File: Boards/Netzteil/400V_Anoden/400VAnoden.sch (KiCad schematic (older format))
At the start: 48 parts, among them P1 Drossel, P2 320V_AC, P3 Stabi, P4 133V_AC, P5 Stabi, P6 Trafo, P7 Trafo, P8 Relay, Q1 2SC2979

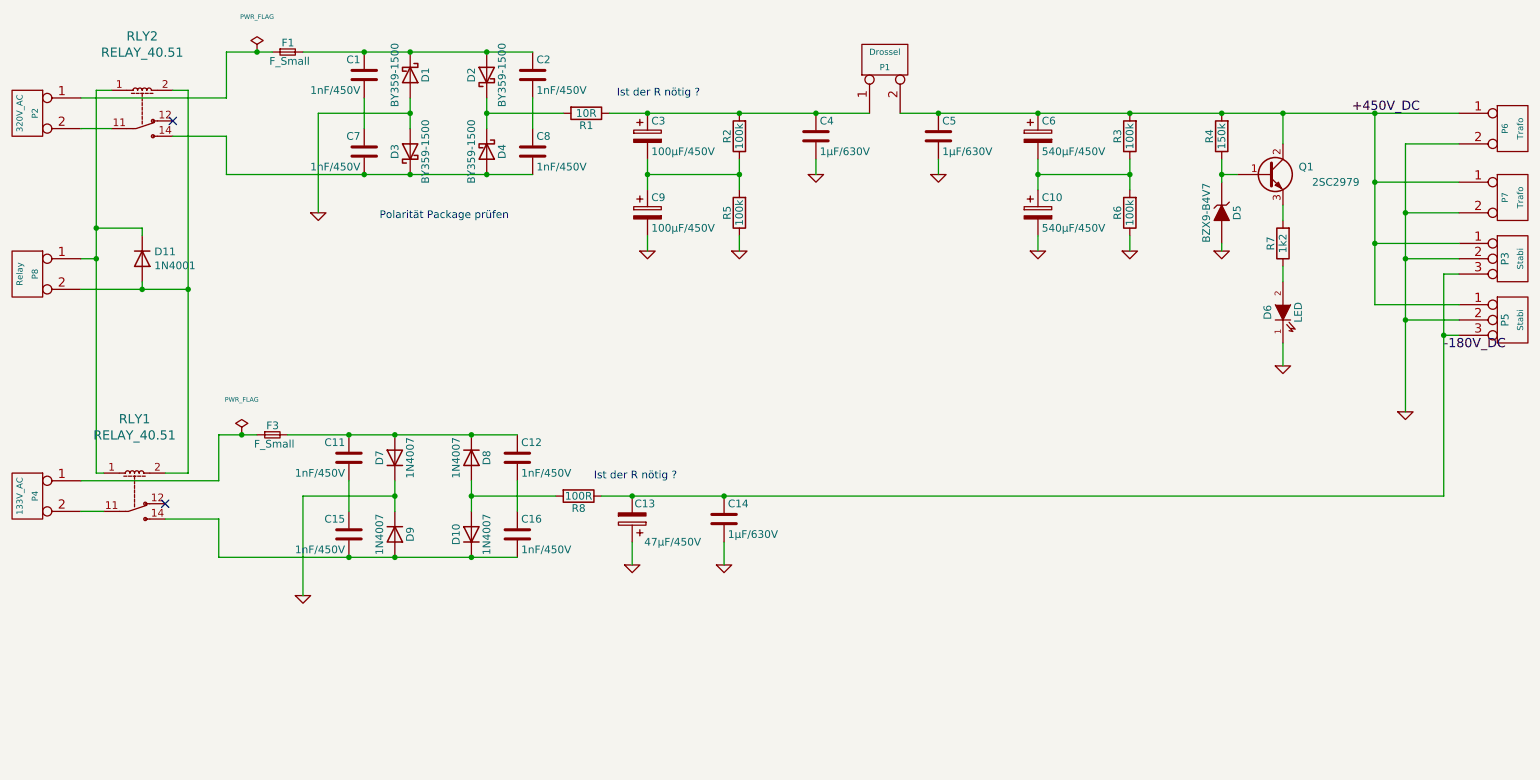
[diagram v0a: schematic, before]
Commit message: Reworked Delay + Layout changed
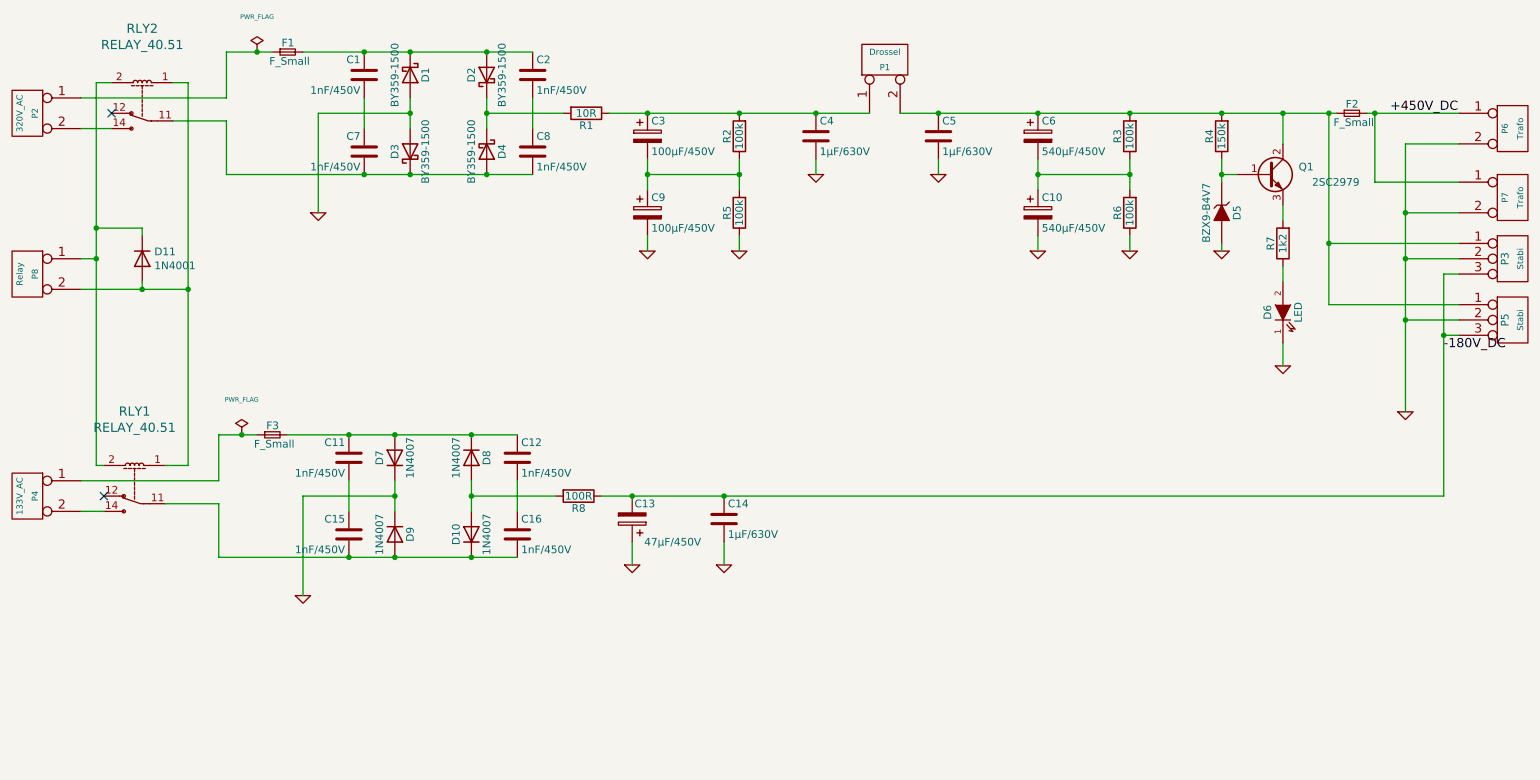
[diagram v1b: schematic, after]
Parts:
- added F2: F_Small, w_misc_comp:fuse_holder_CQ-2, symbol 400VAnoden-rescue:F_Small
- C3: footprint Capacitor_THT:CP_Radial_D18.0mm_P7.50mm -> Capacitor_THT:CP_Radial_D22.0mm_P10.00mm_SnapIn
- Q1: footprint Package_TO_SOT_THT:TO-218-3_Vertical -> Package_TO_SOT_THT:TO-220-3_Horizontal_TabDown
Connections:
- net +450V_DC: now also F2.2; no longer C5.1, C6.1, P1.2 (P2), P3.1 (P1), P5.1 (P1), Q1.2 (C), R3.2, R4.2
- net at P2.2 (P2): now also RLY2.14; no longer RLY2.11
- net at C7.2, C8.2, D3.1 (K)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: now also RLY2.11; no longer RLY2.14
- net at P4.2 (P2): now also RLY1.14; no longer RLY1.11
- net at C15.2, C16.2, D10.1 (K)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: now also RLY1.11; no longer RLY1.14
- net at RLY1.1, RLY2.1: now also D11.2 (A), P8.2 (P2); no longer D11.1 (K), P8.1 (P1)
- net at RLY1.2, RLY2.2: now also D11.1 (K), P8.1 (P1); no longer D11.2 (A), P8.2 (P2)
- new net: C5.1, C6.1, F2.1, P1.2 (P2), P3.1 (P1), P5.1 (P1), Q1.2 (C), R3.2, R4.2
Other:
- note removed: "Ist der R nötig ?"
- note removed: "Polarität Package prüfen"
- moved on the sheet: RLY1, RLY2
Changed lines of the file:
@@
 F 0 "C3" H 5125 2750 50  0000 L CNN
 F 1 "100µF/450V" H 5125 2550 50  0000 L CNN
-F 2 "Capacitor_THT:CP_Radial_D18.0mm_P7.50mm" H 5138 2500 30  0001 C CNN
+F 2 "Capacitor_THT:CP_Radial_D22.0mm_P10.00mm_SnapIn" H 5138 2500 30  0001 C CNN
 F 3 "" H 5100 2650 60  0000 C CNN
 	1    5100 2650
@@
 F 0 "Q1" H 9450 2950 50  0000 R CNN
 F 1 "2SC2979" H 9750 2850 50  0000 R CNN
-F 2 "Package_TO_SOT_THT:TO-218-3_Vertical" H 9350 3000 29  0001 C CNN
+F 2 "Package_TO_SOT_THT:TO-220-3_Horizontal_TabDown" H 9350 3000 29  0001 C CNN
 F 3 "" H 9150 2900 60  0000 C CNN
 	1    9150 2900
@@
 	1    0    0    -1
 $EndComp
-Text Label 9700 2500 0    60   ~ 0
+Text Label 9950 2500 0    60   ~ 0
 +450V_DC
 Text Label 10300 4050 0    60   ~ 0
@@
 Wire Wire Line
 	9250 2500 9250 2700
-Connection ~ 9250 2500
 Wire Wire Line
 	8250 3300 8250 3400
@@
 	3450 4900 3450 5000
 Wire Wire Line
-	9850 3750 10400 3750
+	9550 3750 10400 3750
 $Comp
 L 400VAnoden-rescue:CONN_3-borniers P5
@@
 	6750 2500 7000 2500
 Wire Wire Line
-	10400 3350 9850 3350
-Connection ~ 9850 3350
+	10400 3350 9550 3350
 Wire Wire Line
 	10400 3550 10300 3550
@@
 	8850 2500 9250 2500
 Wire Wire Line
-	9250 2500 9850 2500
-Wire Wire Line
 	5000 5000 4800 5000
 Wire Wire Line
@@
 	3150 4600 3450 4600
 Wire Wire Line
-	9850 3350 9850 3750
+	9550 3350 9550 3750
 $Comp
 L 400VAnoden-rescue:CONN_2-borniers P7
@@
 Wire Wire Line
 	10400 2950 9850 2950
-Connection ~ 9850 2950
-Wire Wire Line
-	9850 2950 9850 3350
 Wire Wire Line
 	10400 2500 9850 2500
-Connection ~ 9850 2500
 Wire Wire Line
 	9850 2500 9850 2950
@@
 L w_relay:RELAY_40.51 RLY1
 U 1 1 5DBE6391
-P 1750 5000
-F 0 "RLY1" H 1750 5503 60  0000 C CNN
-F 1 "RELAY_40.51" H 1750 5397 60  0000 C CNN
-F 2 "w_relay:relay_40.51" H 1750 5000 60  0001 C CNN
-F 3 "" H 1750 5291 60  0000 C CNN
-	1    1750 5000
-	1    0    0    -1
+P 1750 4950
+F 0 "RLY1" H 1750 5453 60  0000 C CNN
+F 1 "RELAY_40.51" H 1750 5347 60  0000 C CNN
+F 2 "w_relay:relay_40.51" H 1750 4950 60  0001 C CNN
+F 3 "" H 1750 5241 60  0000 C CNN
+	1    1750 4950
+	-1   0    0    -1
 $EndComp
 $Comp
 L w_relay:RELAY_40.51 RLY2
 U 1 1 5DBF7BEB
-P 1800 2500
-F 0 "RLY2" H 1800 3003 60  0000 C CNN
-F 1 "RELAY_40.51" H 1800 2897 60  0000 C CNN
-F 2 "w_relay:relay_40.51" H 1800 2500 60  0001 C CNN
-F 3 "" H 1800 2791 60  0000 C CNN
-	1    1800 2500
-	1    0    0    -1
-$EndComp
-Wire Wire Line
-	1600 2350 1500 2350
-Wire Wire Line
-	1500 4850 1550 4850
-Wire Wire Line
-	1950 4850 2100 4850
-Wire Wire Line
-	2100 2350 2000 2350
-Wire Wire Line
-	2100 2350 2100 3650
-Wire Wire Line
-	2100 3650 2100 4850
+P 1800 2450
+F 0 "RLY2" H 1800 2953 60  0000 C CNN
+F 1 "RELAY_40.51" H 1800 2847 60  0000 C CNN
+F 2 "w_relay:relay_40.51" H 1800 2450 60  0001 C CNN
+F 3 "" H 1800 2741 60  0000 C CNN
+	1    1800 2450
+	-1   0    0    -1
+$EndComp
+Wire Wire Line
+	1600 2300 1500 2300
+Wire Wire Line
+	1500 4800 1550 4800
+Wire Wire Line
+	1950 4800 2100 4800
+Wire Wire Line
+	2100 2300 2000 2300
+Wire Wire Line
+	2100 2300 2100 3650
+Wire Wire Line
+	2100 3650 2100 4800
 Connection ~ 2100 3650
 Wire Wire Line
-	1500 2350 1500 3250
+	1500 2300 1500 3250
 Wire Wire Line
 	1400 3650 1800 3650
 Wire Wire Line
-	1500 4850 1500 3450
+	1500 4800 1500 3450
 Connection ~ 1500 3450
 Wire Wire Line
@@
 Wire Wire Line
 	1500 3250 1500 3450
-NoConn ~ 1950 5050
-NoConn ~ 2000 2550
 Wire Wire Line
 	1400 2600 1600 2600
 Wire Wire Line
-	2000 2650 2350 2650
-Wire Wire Line
-	2350 2650 2350 2900
+	2000 2550 2350 2550
+Wire Wire Line
+	2350 2550 2350 2900
 Wire Wire Line
 	1400 2400 2350 2400
@@
 	1550 5100 1400 5100
 Wire Wire Line
-	1950 5150 2300 5150
-Wire Wire Line
-	2300 5150 2300 5400
+	1950 5050 2300 5050
+Wire Wire Line
+	2300 5050 2300 5400
+Wire Wire Line
+	2300 4900 2300 4600
 Wire Wire Line
 	1400 4900 2300 4900
-Wire Wire Line
-	2300 4900 2300 4600
-Text Notes 4900 2400 0    50   ~ 0
-Ist der R nötig ?
-Text Notes 4750 4900 0    50   ~ 0
-Ist der R nötig ?
-Text Notes 3350 3200 0    50   ~ 0
-Polarität Package prüfen
+$Comp
+L 400VAnoden-rescue:F_Small F2
+U 1 1 608CDC13
+P 9700 2500
+F 0 "F2" H 9660 2560 50  0000 L CNN
+F 1 "F_Small" H 9580 2440 50  0000 L CNN
+F 2 "w_misc_comp:fuse_holder_CQ-2" H 9700 2500 60  0001 C CNN
+F 3 "" H 9700 2500 60  0000 C CNN
+	1    9700 2500
+	1    0    0    -1
+$EndComp
+Wire Wire Line
+	9550 3350 9550 2500
+Wire Wire Line
+	9550 2500 9250 2500
+Connection ~ 9550 3350
+Connection ~ 9250 2500
+Wire Wire Line
+	9600 2500 9550 2500
+Connection ~ 9550 2500
+Wire Wire Line
+	9800 2500 9850 2500
+Connection ~ 9850 2500
+NoConn ~ 1550 5000
+NoConn ~ 1600 2500
 $EndSCHEMATC

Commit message: Work in progess - many LAyour changes
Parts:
- added J1: Chassis_GND, MountingHole:MountingHole_3.2mm_M3_Pad_Via, symbol Connector:Screw_Terminal_01x01
- F2: value F_Small -> 500mAT
- P5: footprint Connector_TE-Connectivity:TE_MATE-N-LOK_1-770870-x_1x03_P4.14mm_Vertical -> footprints:39302030
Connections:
- net GND: now also J1.1 (Pin_1)
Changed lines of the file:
@@
 F 0 "P5" V 10700 3850 50  0000 C CNN
 F 1 "Stabi" V 10800 3850 40  0000 C CNN
-F 2 "Connector_TE-Connectivity:TE_MATE-N-LOK_1-770870-x_1x03_P4.14mm_Vertical" H 10750 3850 60  0001 C CNN
+F 2 "footprints:39302030" H 10750 3850 60  0001 C CNN
 F 3 "" H 10750 3850 60  0001 C CNN
 	1    10750 3850
@@
 P 9700 2500
 F 0 "F2" H 9660 2560 50  0000 L CNN
-F 1 "F_Small" H 9580 2440 50  0000 L CNN
+F 1 "500mAT" H 9580 2440 50  0000 L CNN
 F 2 "w_misc_comp:fuse_holder_CQ-2" H 9700 2500 60  0001 C CNN
 F 3 "" H 9700 2500 60  0000 C CNN
@@
 NoConn ~ 1550 5000
 NoConn ~ 1600 2500
+$Comp
+L Connector:Screw_Terminal_01x01 J1
+U 1 1 60D32E1A
+P 1450 6200
+F 0 "J1" V 1414 6112 50  0000 R CNN
+F 1 "Chassis_GND" V 1323 6112 50  0000 R CNN
+F 2 "MountingHole:MountingHole_3.2mm_M3_Pad_Via" H 1450 6200 50  0001 C CNN
+F 3 "~" H 1450 6200 50  0001 C CNN
+	1    1450 6200
+	0    -1   -1   0
+$EndComp
+$Comp
+L power:GND #PWR0101
+U 1 1 60D42140
+P 1450 6550
+F 0 "#PWR0101" H 1450 6300 50  0001 C CNN
+F 1 "GND" H 1455 6377 50  0000 C CNN
+F 2 "" H 1450 6550 50  0001 C CNN
+F 3 "" H 1450 6550 50  0001 C CNN
+	1    1450 6550
+	1    0    0    -1
+$EndComp
+Wire Wire Line
+	1450 6550 1450 6400
 $EndSCHEMATC
